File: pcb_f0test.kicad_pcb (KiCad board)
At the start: 2 copper layers, 50 x 50 mm, 88 parts, among them P1 CONN_02X05, P2 CONN_01X02, P3 CONN_01X06, P5 CONN_02X05, P6 CONN_02X05, P7 CONN_01X01, P8 CONN_01X01, U1 STM32F042GxU, U2 LP2985LV, U3 KNUSB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

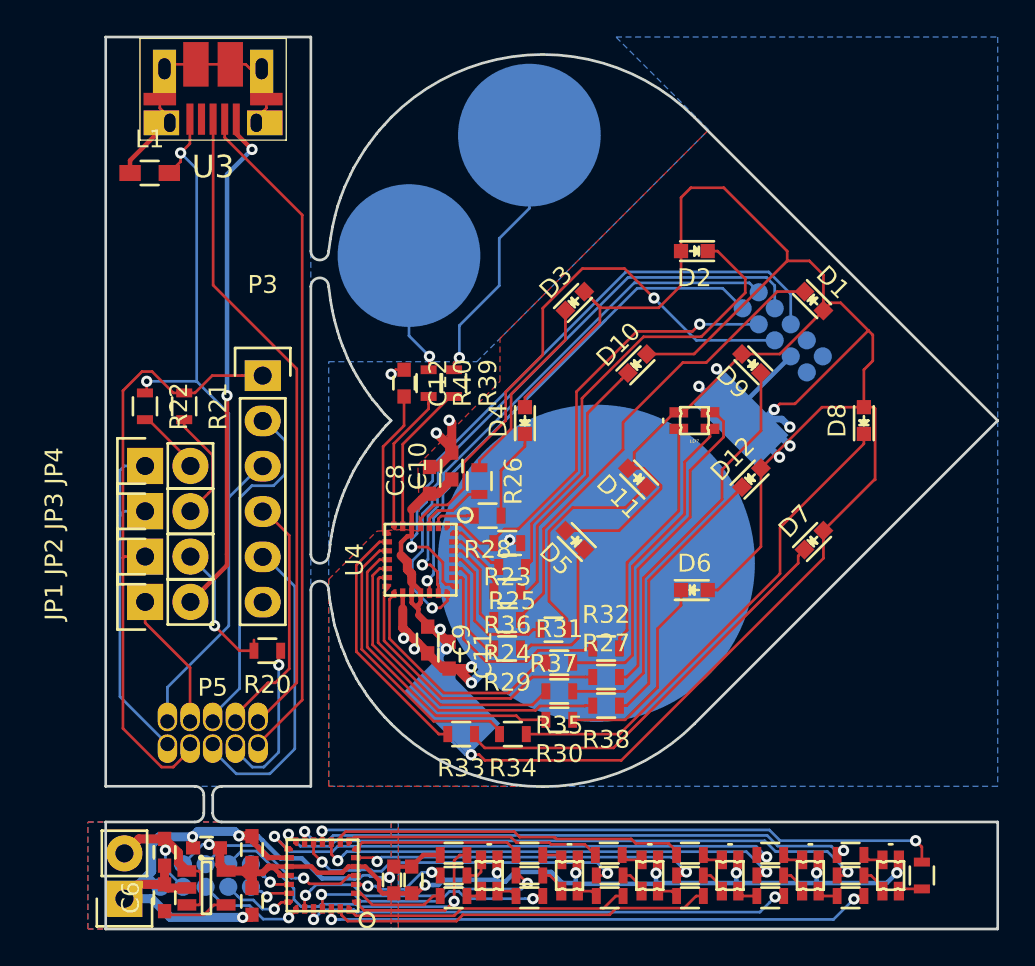
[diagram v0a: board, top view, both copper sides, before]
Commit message: Routing cleanup and silkscreen on heart.
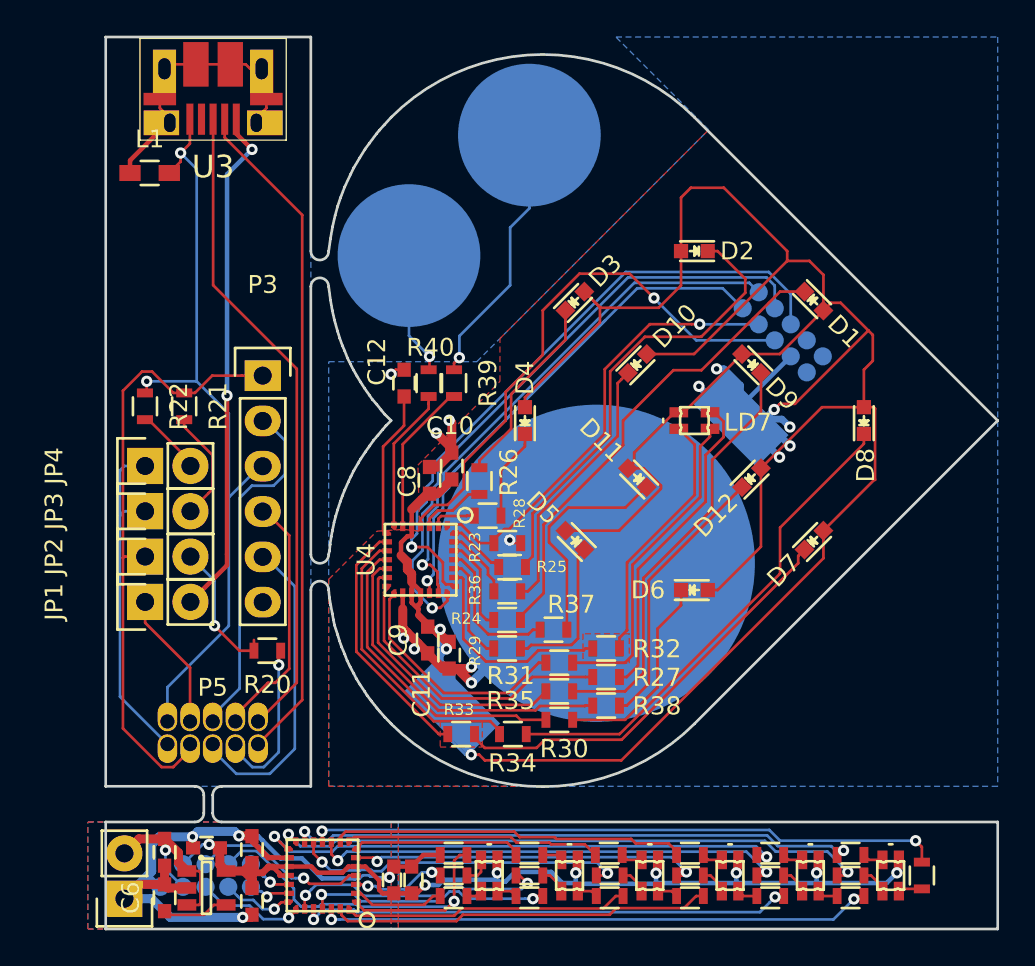
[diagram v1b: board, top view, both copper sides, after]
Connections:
- BT1 pad 1: +3V3 -> +2V5
- C10 pad 1: +3V3 -> +2V5
- C11 pad 1: +3V3 -> +2V5
- C8 pad 1: +3V3 -> +2V5
- C9 pad 1: +3V3 -> +2V5
- D1 pad 2: +3V3 -> +2V5
- D10 pad 2: +3V3 -> +2V5
- D11 pad 2: +3V3 -> +2V5
- D12 pad 2: +3V3 -> +2V5
- D2 pad 2: +3V3 -> +2V5
- D3 pad 2: +3V3 -> +2V5
- D4 pad 2: +3V3 -> +2V5
- D5 pad 2: +3V3 -> +2V5
- D6 pad 2: +3V3 -> +2V5
- D7 pad 2: +3V3 -> +2V5
- D8 pad 2: +3V3 -> +2V5
- D9 pad 2: +3V3 -> +2V5
- LD7 pad 1: +3V3 -> +2V5
- P1 pad 4: +3V3 -> +2V5
- U4 pad 17: +3V3 -> +2V5
- U4 pad 18: +3V3 -> +2V5
- U4 pad 5: +3V3 -> +2V5
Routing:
- net +2V5: track 0.00 -> 180.3 mm, vias 0 -> 9
- net +3V3: track 235.6 -> 55.5 mm, vias 17 -> 8
- net /sheet_heart/h_ildb1: track 13.7 -> 14.4 mm
- added copper zone on F.Cu, net +2V5

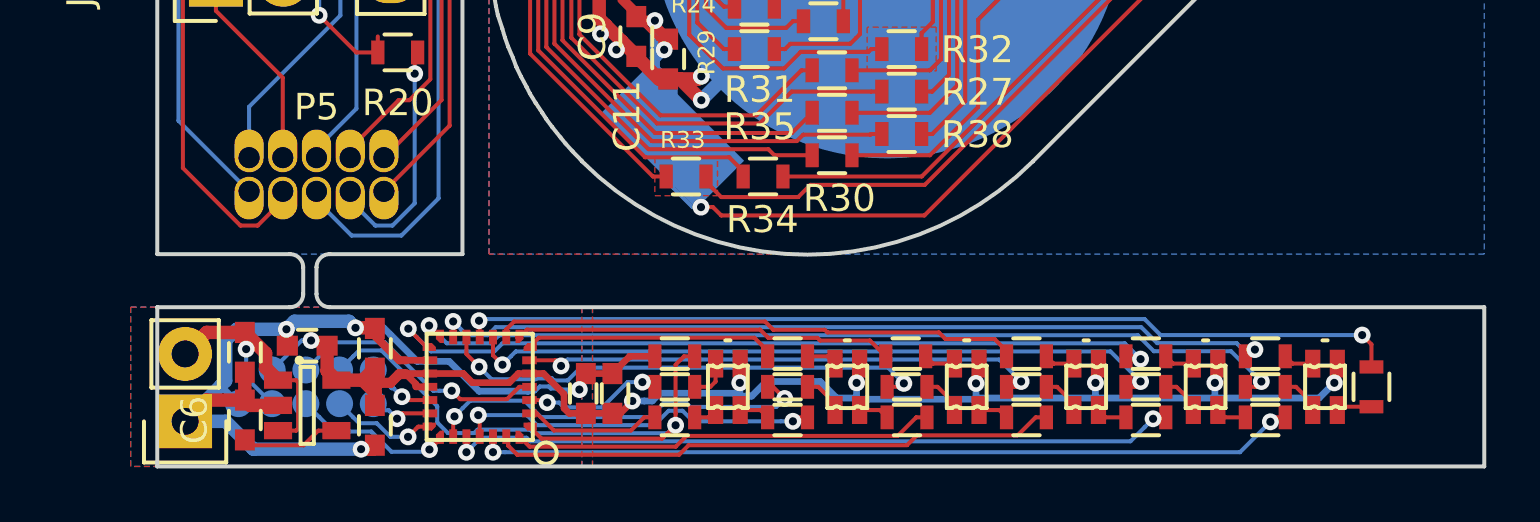
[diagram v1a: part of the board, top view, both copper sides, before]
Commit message: Tweak outline of ring PCB.
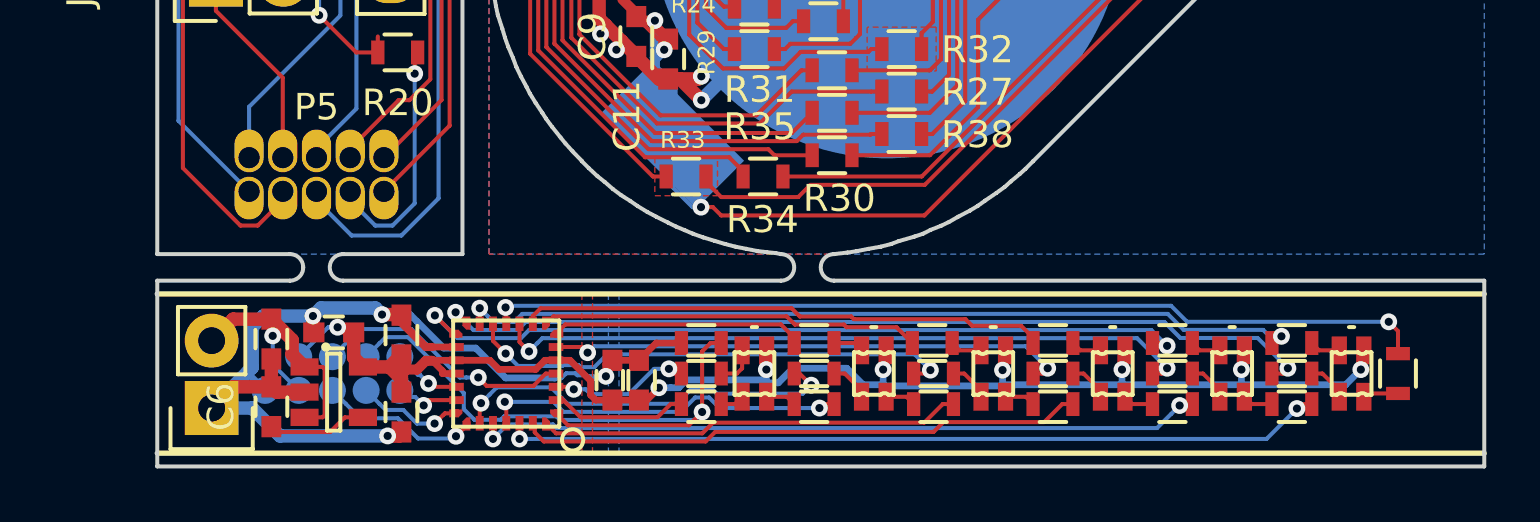
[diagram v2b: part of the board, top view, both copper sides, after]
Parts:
- moved R14 1.12 mm to (65.2, 63.6)
- moved R15 1.12 mm to (69.8, 63.6)
- moved R3 1.12 mm to (51.8, 63.6)
- moved R5 1.12 mm to (47.5, 63.6)
- moved R8 1.12 mm to (56.2, 63.6)
- moved R9 1.12 mm to (60.8, 63.6)
- moved C1 1.12 mm to (36.2, 61.0)
- moved C2 1.12 mm to (44.1, 62.8)
- moved C3 1.12 mm to (36.2, 64.0)
- moved C4 1.12 mm to (45.1, 62.8)
- moved C5 1.12 mm to (31.3, 61.2)
- moved C6 1.12 mm to (31.3, 63.8)
- moved C7 1.12 mm to (33.6, 61.0)
- moved LD1 1.12 mm to (49.5, 62.5)
- moved LD2 1.12 mm to (54.0, 62.5)
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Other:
- outline, holes or cut-outs redrawn

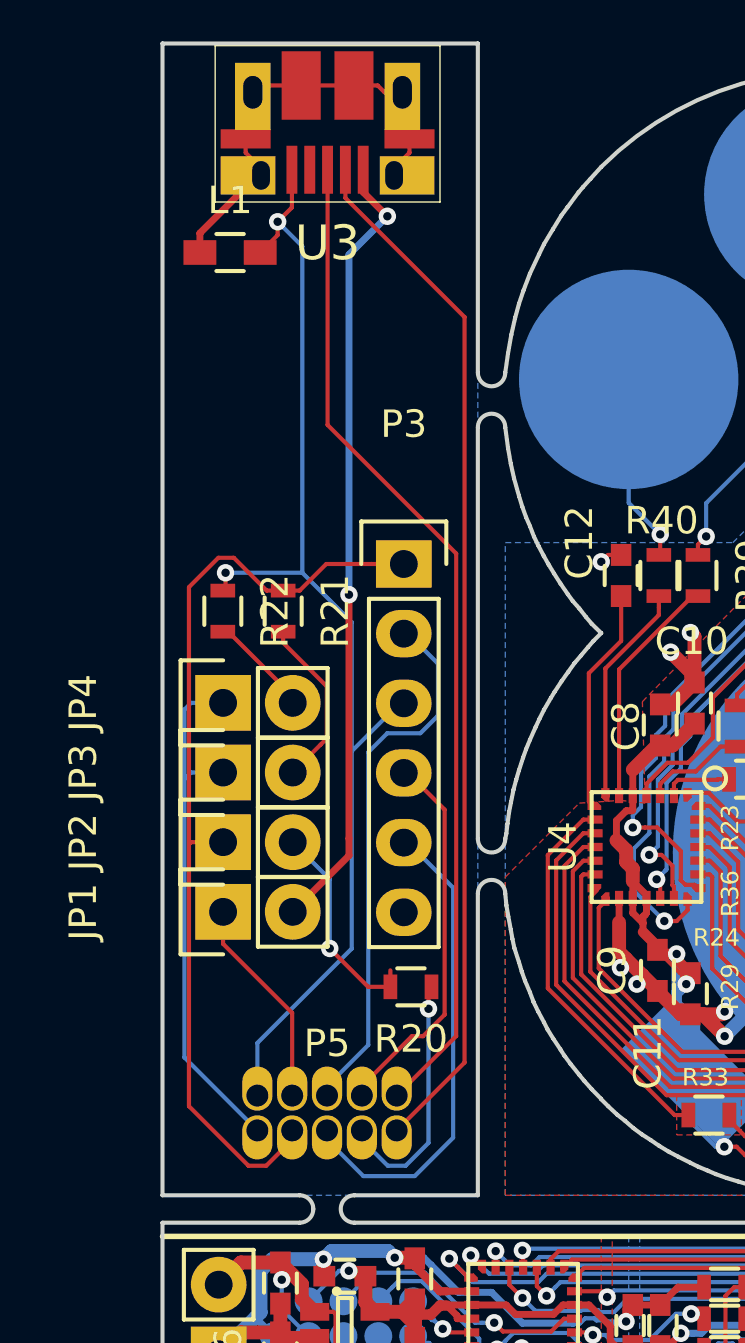
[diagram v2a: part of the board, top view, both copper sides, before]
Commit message: New routing of pogo-pins board (still needs some cleanup).
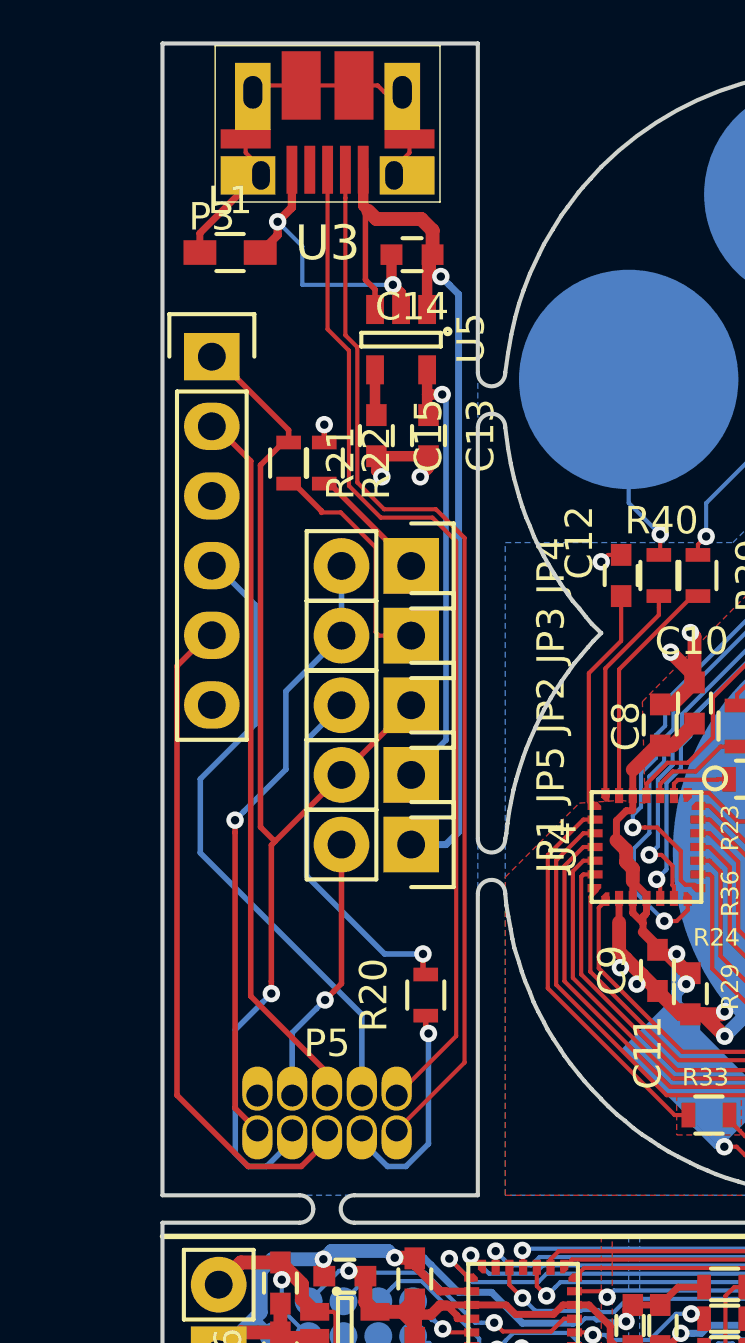
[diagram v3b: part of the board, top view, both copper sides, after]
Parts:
- added C13: 2.2u, Capacitors_SMD:C_0603, F.Cu at (36.7, 30.3)
- added C14: 1u, Capacitors_SMD:C_0603, F.Cu at (36.1, 23.7)
- added C15: 10n, Capacitors_SMD:C_0603, F.Cu at (34.8, 30.3)
- added JP5: Jumper_NC_Small, Pin_Headers:Pin_Header_Straight_1x02, F.Cu at (36.1, 42.7)
- added U5: LP2985LV, TO_SOT_Packages_SMD:SOT-23-5, F.Cu at (35.7, 26.8)
- moved P3 10.3 mm to (28.8, 27.4)
- moved JP2 8.48 mm to (36.1, 40.1), turned to 270 degrees
- moved JP3 8.48 mm to (36.1, 37.6), turned to 270 degrees
- moved JP4 8.48 mm to (36.1, 35.1), turned to 270 degrees
- moved JP1 7.28 mm to (36.1, 45.2), turned to 270 degrees
- moved R22 6.55 mm to (32.9, 31.3)
- moved R21 5.40 mm to (31.6, 31.3)
- moved R20 0.62 mm to (36.6, 50.7), turned to 90 degrees
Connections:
- JP1 pad 1: /sheet_pogopins/pogo_vbus -> /sheet_pogopins/usb_vbus
- JP1 pad 2: /sheet_pogopins/usb_vbus -> /sheet_pogopins/pogo_vbus
- JP4 pad 1: Net-(JP3-Pad1) -> Net-(JP4-Pad1)
- JP4 pad 2: Net-(JP4-Pad2) -> Net-(JP3-Pad2)
- P5 pad 2: Net-(JP3-Pad1) -> Net-(JP3-Pad2)
- R21 pad 2: Net-(JP3-Pad2) -> Net-(JP3-Pad1)
- R22 pad 2: Net-(JP4-Pad2) -> Net-(JP4-Pad1)
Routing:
- net /sheet_pogopins/pogo_gnd: track 44.0 -> 15.9 mm, vias 2 -> 5
- net Net-(C13-Pad1): track 0.00 -> 16.7 mm, vias 0 -> 1
- net Net-(JP3-Pad2): track 6.31 -> 22.5 mm, vias 0 -> 1
- net Net-(JP3-Pad1): track 19.5 -> 8.60 mm
- net /sheet_pogopins/tg_swdio: track 14.0 -> 23.7 mm
- net /sheet_pogopins/tg_nrst: track 17.7 -> 24.7 mm
- net /sheet_pogopins/tg_pwr: track 34.8 -> 41.7 mm, vias 0 -> 1
- net /sheet_pogopins/tg_swclk: track 19.8 -> 26.2 mm
- net /sheet_pogopins/usb_vbus: track 28.9 -> 34.4 mm, vias 2 -> 1
- net Net-(JP2-Pad2): track 7.83 -> 13.0 mm
- net Net-(JP4-Pad1): track 0.00 -> 4.43 mm
- net Net-(JP4-Pad2): track 3.77 -> 0.00 mm
- net /sheet_pogopins/pogo_vbus: track 7.74 -> 9.90 mm, vias 0 -> 1
- net /sheet_pogopins/pogo_bypass: track 0.00 -> 1.67 mm
- net /sheet_pogopins/pogo_dm: track 37.9 -> 39.0 mm
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
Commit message: Cleanup routing on pogo-pins pcb, looks good now.
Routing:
- net /sheet_pogopins/tg_swclk: track 26.2 -> 28.7 mm, vias 0 -> 2
- net /sheet_pogopins/tg_nrst: track 24.7 -> 25.7 mm
- net Net-(JP2-Pad2): track 13.0 -> 12.5 mm
- net /sheet_pogopins/tg_swdio: track 23.7 -> 23.9 mm, vias 0 -> 2
- net /sheet_pogopins/tg_pwr: track 41.7 -> 41.6 mm, vias 1 -> 0

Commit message: Silkscreen and cleanup.
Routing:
- net /sheet_heart/h_usb_dm: track 40.8 -> 29.0 mm
- net /sheet_heart/h_ild5: track 25.9 -> 24.7 mm
- net /sheet_heart/h_boot0: track 25.2 -> 26.3 mm
- net /sheet_heart/h_swclk: track 35.7 -> 36.2 mm
- net /sheet_heart/h_usb_dp: track 30.1 -> 30.7 mm
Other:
- outline, holes or cut-outs redrawn
- board text added: "3V3"
- board text added: "5V"
- board text added: "B0"
- board text added: "H"
- board text added: "L"
- board text added: "r"
- board text added: "tx"

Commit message: More silk screen, getting pretty close now, I think.
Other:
- board text added: "LED-heart rev1 knielsen-hq.org/led-heart/"
- board text added: "LED-ring rev1 knielsen-hq.org/led-ring/"
- board text added: "Pogo-Elf rev1 knielsen-hq.org/pogo-elf/"
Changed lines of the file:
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@@
     (area 26.924999 15.924999 77.075001 66.075001)
     (thickness 0.8)
-    (drawings 176)
+    (drawings 179)
     (tracks 1093)
     (zones 0)
@@
     )
   )
+  (gr_text "Pogo-Elf rev1\nknielsen-hq.org/pogo-elf/" (at 32.3 22.4 270) (layer B.SilkS)
+    (effects (font (size 1.2 1) (thickness 0.2)) (justify right mirror))
+  )
+  (gr_text "LED-heart rev1\nknielsen-hq.org/led-heart/" (at 51.4 31.4 45) (layer B.SilkS)
+    (effects (font (size 1.5 1.2) (thickness 0.25)) (justify mirror))
+  )
+  (gr_text "LED-ring rev1\nknielsen-hq.org/led-ring/" (at 73.2 62.5) (layer B.SilkS)
+    (effects (font (size 1.5 1.25) (thickness 0.275)) (justify left mirror))
+  )
   (gr_arc (start 37 17.5) (end 37 16) (angle 90) (layer Edge.Cuts) (width 0.15))
